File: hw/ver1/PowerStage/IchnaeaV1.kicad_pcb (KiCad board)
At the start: 4 copper layers, 96.5 x 96.5 mm, 202 parts, among them J2 Conn_02x12_Odd_Even, J3 Screw_Terminal_01x09, J4 Screw_Terminal_01x09, J5 Screw_Terminal_01x09, J6 Screw_Terminal_01x09, J7 Conn_01x02_Socket, J8 FanConnector, Q1 MCAC80N10Y, Q10 MCAC80N10Y, Q11 MCAC80N10Y, Q12 MCAC80N10Y, Q13 MCAC80N10Y, Q14 MCAC80N10Y, Q15 MCAC80N10Y, Q16 MCAC80N10Y, Q2 MCAC80N10Y, Q3 BSS138, Q4 BSS138, Q5 BSS84, Q6 BSS138, Q7 MCAC80N10Y, Q8 MCAC80N10Y, Q9 MCAC80N10Y, SW1 SW_DIP_x03, U1 HIP2210, U2 74HC4051PW, U3 LTC7871, U4 LM1117MP-3.3, U5 HIP2210, U6 HIP2210, U7 HIP2210, U8 HIP2210, U9 HIP2210

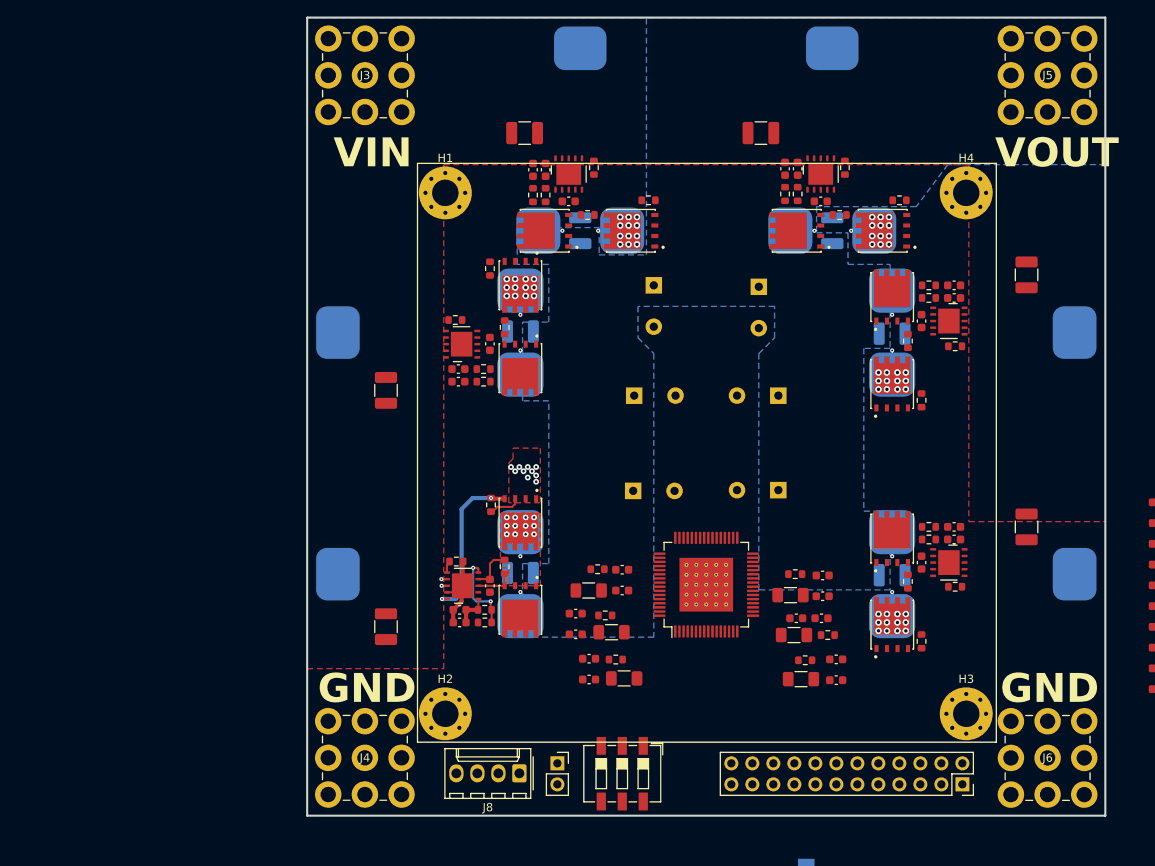
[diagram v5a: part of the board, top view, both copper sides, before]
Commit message: More power plane work. Double mosfets.
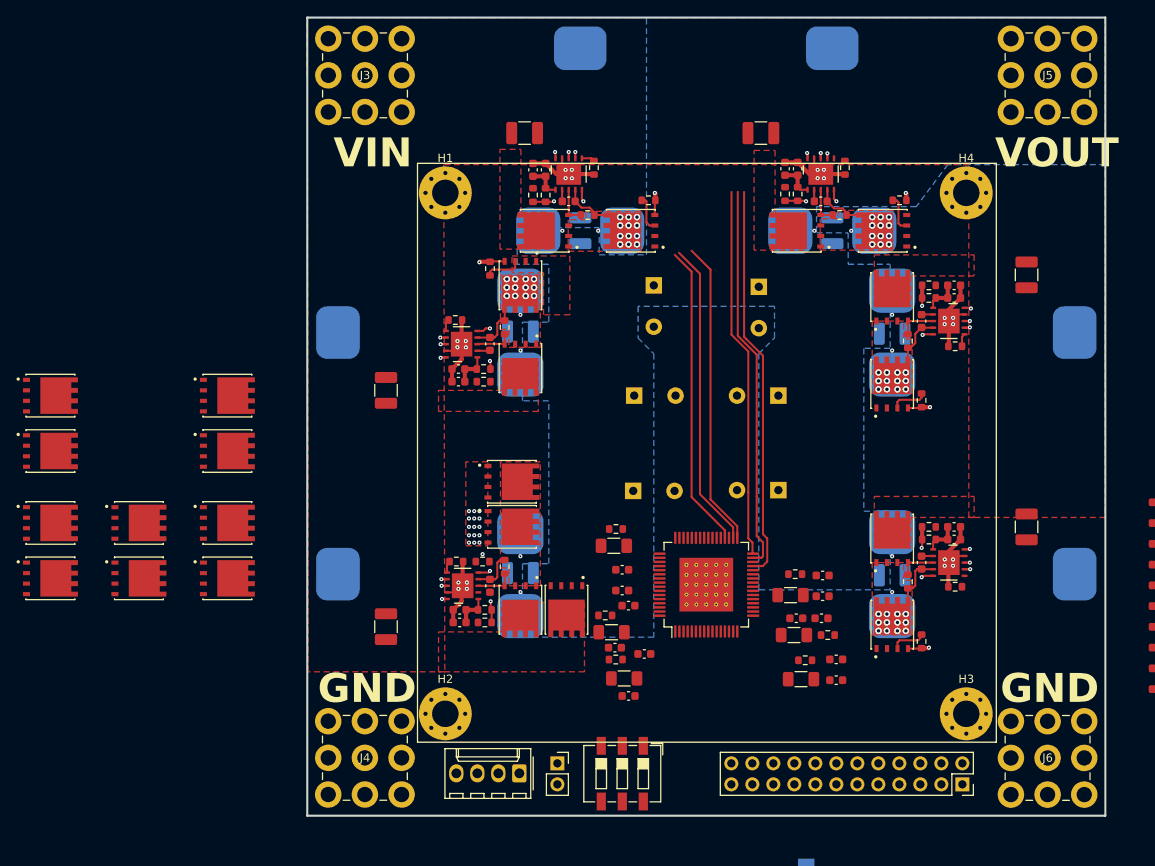
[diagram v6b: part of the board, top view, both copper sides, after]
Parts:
- added Q17: MCAC80N10Y, Mosfets:TRANS_BSC076N06NS3-G, F.Cu at (70.5, 96.5)
- added Q18: MCAC80N10Y, Mosfets:TRANS_BSC076N06NS3-G, F.Cu at (81.2, 111.9)
- added Q19: MCAC80N10Y, Mosfets:TRANS_BSC076N06NS3-G, F.Cu at (91.9, 96.5)
- added Q20: MCAC80N10Y, Mosfets:TRANS_BSC076N06NS3-G, F.Cu at (91.9, 111.9)
- added Q21: MCAC80N10Y, Mosfets:TRANS_BSC076N06NS3-G, F.Cu at (70.5, 111.9)
- added Q22: MCAC80N10Y, Mosfets:TRANS_BSC076N06NS3-G, F.Cu at (133.0, 122.4)
- added Q23: MCAC80N10Y, Mosfets:TRANS_BSC076N06NS3-G, F.Cu at (70.5, 103.2)
- added Q24: MCAC80N10Y, Mosfets:TRANS_BSC076N06NS3-G, F.Cu at (81.2, 118.6)
- added Q25: MCAC80N10Y, Mosfets:TRANS_BSC076N06NS3-G, F.Cu at (91.9, 103.2)
- added Q26: MCAC80N10Y, Mosfets:TRANS_BSC076N06NS3-G, F.Cu at (91.9, 118.6)
- added Q27: MCAC80N10Y, Mosfets:TRANS_BSC076N06NS3-G, F.Cu at (70.5, 118.6)
- added Q28: MCAC80N10Y, Mosfets:TRANS_BSC076N06NS3-G, F.Cu at (126.3, 106.9)
- moved C50 8.63 mm to (142.4, 127.8)
- moved R76 6.93 mm to (122.8, 116.6), turned to 0 degrees
- moved C55 6.56 mm to (140.5, 132.8)
- moved C49 6.45 mm to (140.4, 121.9)
- moved R68 6.21 mm to (138.7, 114.7)
- moved R69 5.35 mm to (138.9, 112.6)
- moved C56 4.96 mm to (138.8, 127.0)
- moved Q16 1.14 mm to (126.4, 112.4), turned to 0 degrees
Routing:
- net GND: track 14.0 -> 85.3 mm, vias 10 -> 39
- net /PowerStage/Phase1/PWM: track 0.00 -> 48.4 mm, vias 0 -> 1
- net /PowerStage/Phase2/PWM: track 0.00 -> 47.2 mm, vias 0 -> 1
- net /PowerStage/Phase3/PWM: track 0.00 -> 45.5 mm, vias 0 -> 1
- net /PowerStage/Phase5/PWM: track 0.00 -> 37.8 mm, vias 0 -> 1
- net /PowerStage/Phase4/PWM: track 0.00 -> 37.8 mm, vias 0 -> 1
- net /PowerStage/Phase6/PWM: track 0.65 -> 37.4 mm
- net +VSW: track 4.30 -> 25.8 mm
- net Net-(Q24-G): track 0.00 -> 20.9 mm, vias 0 -> 2
- net Net-(Q12-G): track 0.00 -> 20.8 mm, vias 0 -> 2
- net Net-(Q14-G): track 0.00 -> 20.5 mm, vias 0 -> 2
- net Net-(Q2-G): track 0.00 -> 20.4 mm, vias 0 -> 2
- net Net-(Q10-G): track 0.00 -> 19.2 mm, vias 0 -> 2
- net Net-(Q16-G): track 19.2 -> 11.2 mm
- net Net-(U6-VREF): track 0.00 -> 7.76 mm, vias 0 -> 2
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- added copper zone on F.Cu, net Net-(Q1-S)
- added copper zone on F.Cu, net Net-(Q10-D)
- added copper zone on F.Cu, net Net-(Q11-S)
- added copper zone on F.Cu, net Net-(Q13-S)
- added copper zone on F.Cu, net Net-(Q18-S)

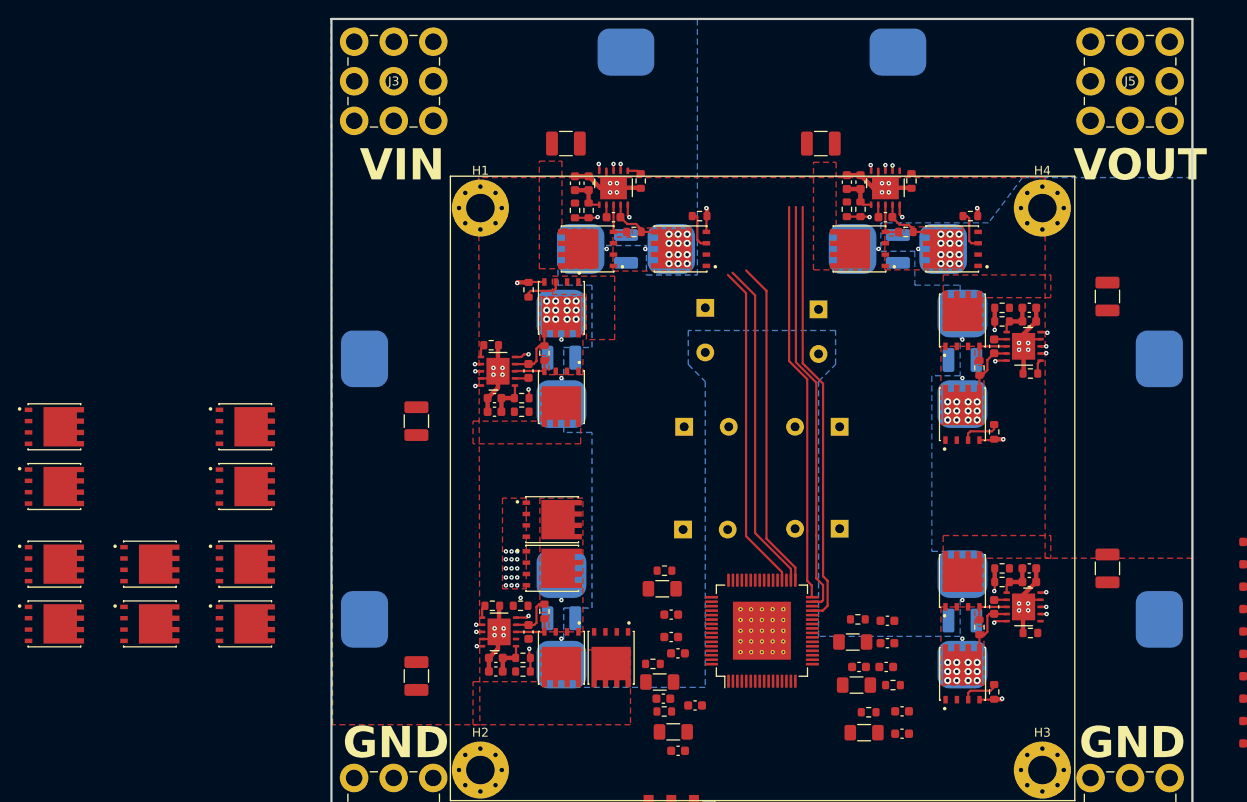
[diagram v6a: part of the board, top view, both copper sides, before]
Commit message: Improve power routing
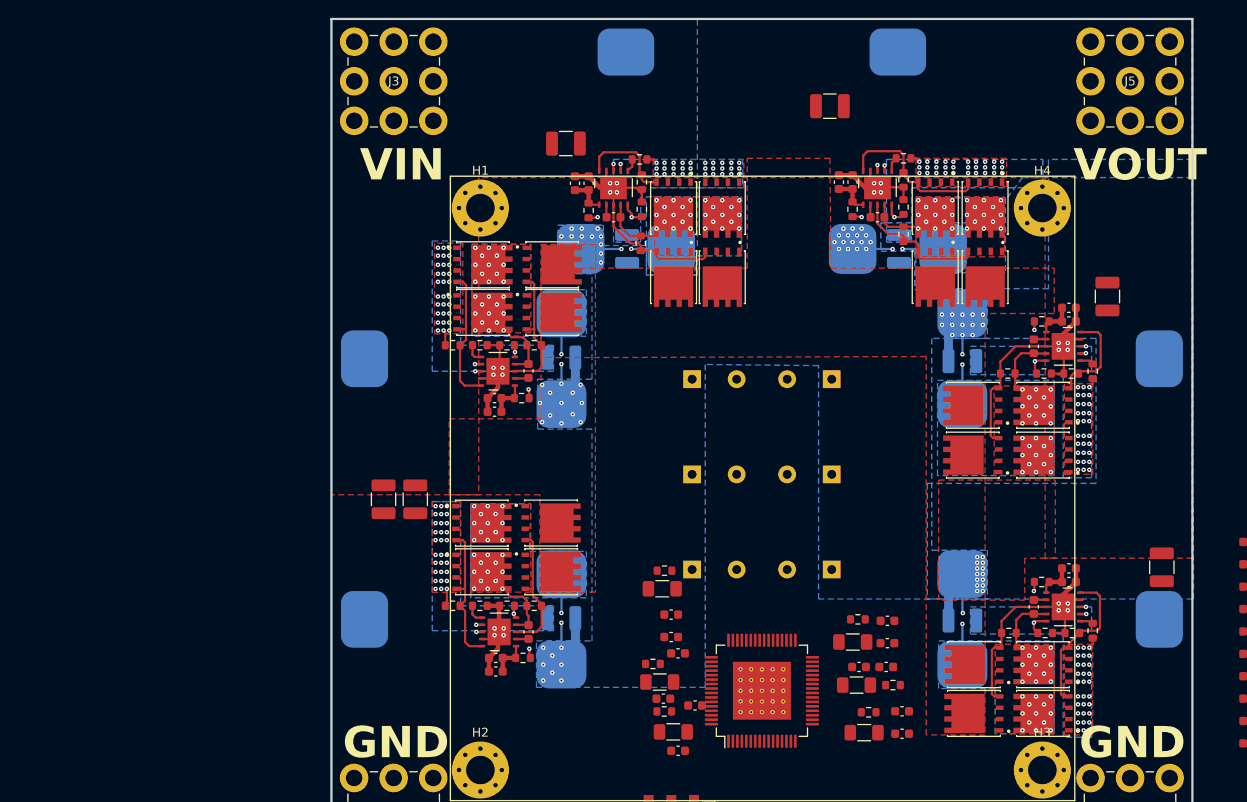
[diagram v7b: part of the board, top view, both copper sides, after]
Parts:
- moved Q23 113.7 mm to (181.4, 128.7), turned to 180 degrees
- moved Q17 108.0 mm to (173.6, 128.7), turned to 180 degrees
- moved Q24 101.9 mm to (181.4, 99.7), turned to 180 degrees
- moved Q18 93.1 mm to (173.5, 99.7), turned to 180 degrees
- moved Q25 88.6 mm to (174.9, 72.0), turned to -90 degrees
- moved Q19 84.6 mm to (174.9, 79.8), turned to -90 degrees
- moved Q26 70.9 mm to (145.4, 72.0), turned to -90 degrees
- moved Q21 65.1 mm to (126.3, 78.4)
- moved Q27 62.7 mm to (118.6, 78.4)
- moved Q20 62.4 mm to (145.4, 79.8), turned to -90 degrees
- moved C59 20.2 mm to (107.4, 104.6), turned to -90 degrees
- moved Q22 16.5 mm to (126.2, 107.3), turned to 0 degrees
- moved R2 11.0 mm to (184.7, 119.6), turned to 0 degrees
- moved R56 10.8 mm to (184.5, 90.6), turned to 0 degrees
- moved R71 10.5 mm to (115.2, 87.4), turned to 0 degrees
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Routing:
- net /PowerStage/Phase1/PWM: track 48.4 -> 0.64 mm
- net /PowerStage/Phase2/PWM: track 47.2 -> 0.64 mm
- net /PowerStage/Phase3/PWM: track 45.5 -> 0.64 mm
- net /PowerStage/Phase5/PWM: track 37.8 -> 0.64 mm
- net /PowerStage/Phase4/PWM: track 37.8 -> 0.77 mm
- net /PowerStage/Phase6/PWM: track 37.4 -> 0.65 mm
- net VLOW: track 215.5 -> 242.3 mm, vias 6 -> 81
- net Net-(Q18-G): track 4.64 -> 16.0 mm
- net Net-(Q19-G): track 4.52 -> 15.8 mm
- net Net-(Q1-G): track 4.52 -> 15.7 mm
- net Net-(Q11-G): track 4.52 -> 15.6 mm
- net Net-(Q13-G): track 4.55 -> 14.7 mm
- net Net-(Q15-G): track 4.65 -> 14.8 mm
- net Net-(Q12-G): track 20.8 -> 11.0 mm, vias 2 -> 0
- net Net-(Q24-G): track 20.9 -> 11.2 mm, vias 2 -> 0
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- added copper zone on B.Cu, net GND
- added copper zone on B.Cu, net Net-(Q1-S)
- added copper zone on B.Cu, net Net-(Q10-D)
- added copper zone on B.Cu, net Net-(Q11-S)
- added copper zone on B.Cu, net Net-(Q13-S)
- added copper zone on B.Cu, net Net-(Q15-S)
- added copper zone on B.Cu, net Net-(Q18-S)
- added copper zone on In1.Cu, net VLOW
- removed copper zone on In1.Cu, net HT
- removed copper zone on In2.Cu, net VLOW

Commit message: Sync effort from before work
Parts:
- moved C58 30.3 mm to (190.6, 112.1)
- moved C19 15.1 mm to (172.1, 64.3)
- moved C23 14.7 mm to (142.6, 64.4), turned to 180 degrees
- moved C20 0.40 mm to (194.3, 112.1)
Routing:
- net +VSW: track 25.8 -> 167.3 mm, vias 0 -> 6
- net /PowerStage/Phase1/PWMEN: track 4.05 -> 144.9 mm
- net /PowerStage/Phase6/PWM: track 0.65 -> 93.2 mm
- net /PowerStage/Phase1/PWM: track 0.64 -> 79.7 mm
- net /PowerStage/Phase5/PWM: track 0.64 -> 61.0 mm
- net /PowerStage/Phase2/PWM: track 0.64 -> 51.6 mm
- net /PowerStage/Phase4/PWM: track 0.77 -> 23.7 mm
- net /PowerStage/Phase3/PWM: track 0.64 -> 11.9 mm
- net GND: track 82.5 -> 89.0 mm
- net Net-(U8-VREF): track 7.17 -> 7.75 mm
- net VLOW: track 242.3 -> 242.1 mm, vias 81 -> 90
